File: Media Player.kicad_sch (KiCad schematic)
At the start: 74 parts, among them J1 PH2.0, J2 MEM2075-00-140-01-A, J3 USB_C_Receptacle_USB2.0_16P, J4 UART, Q2 DMP3068L-7, Q3 DMP3068L-7, SW1 BOOT, SW2 RESET, SW3 SW_Push, SW4 SW_Push, SW5 SW_Push, SW6 SW_Push, SW7 SW_SPST, U1 ESP32-S3-WROOM-1

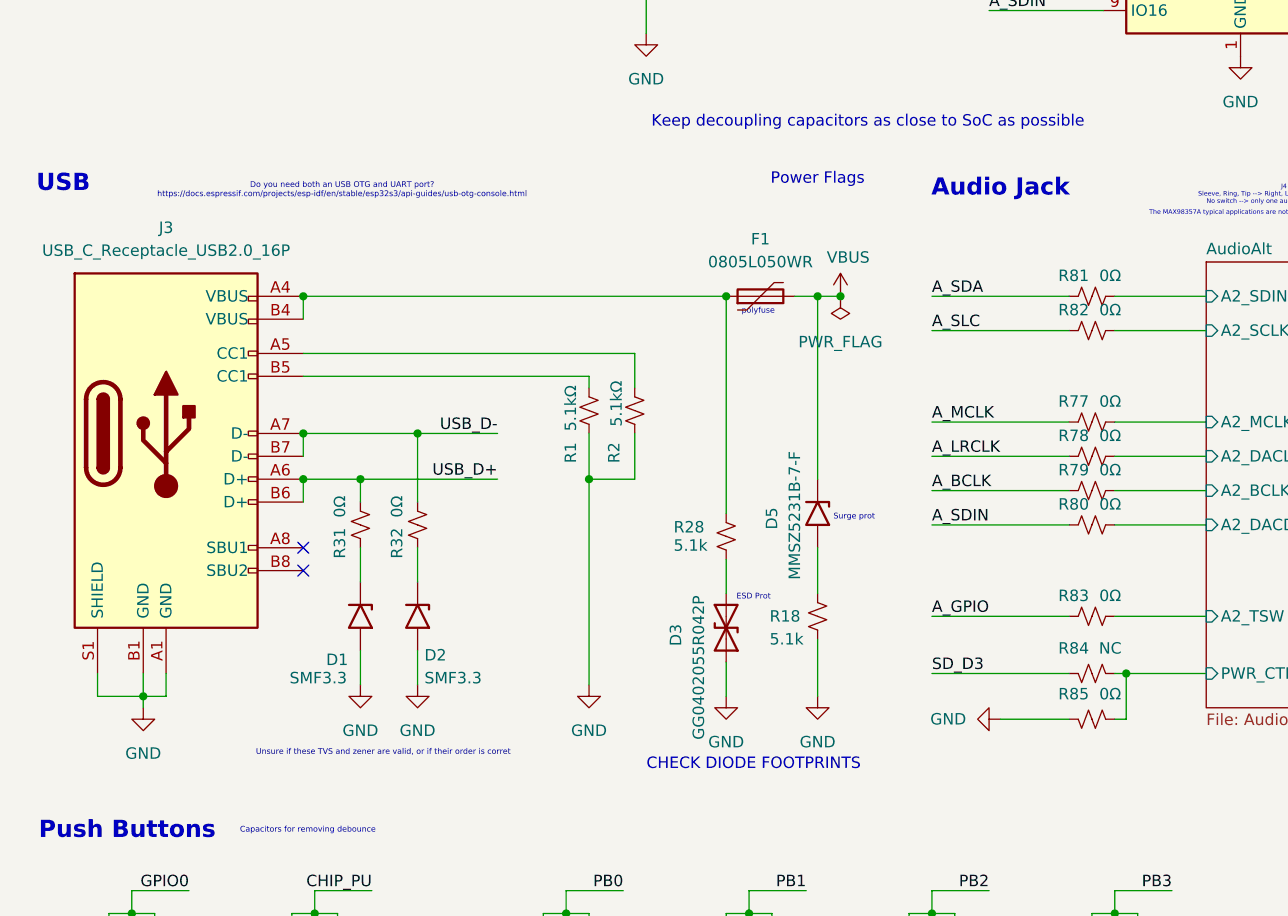
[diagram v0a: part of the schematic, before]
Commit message: Small Change to USB routing
Removed 0 resistors and change components to match reference schematic
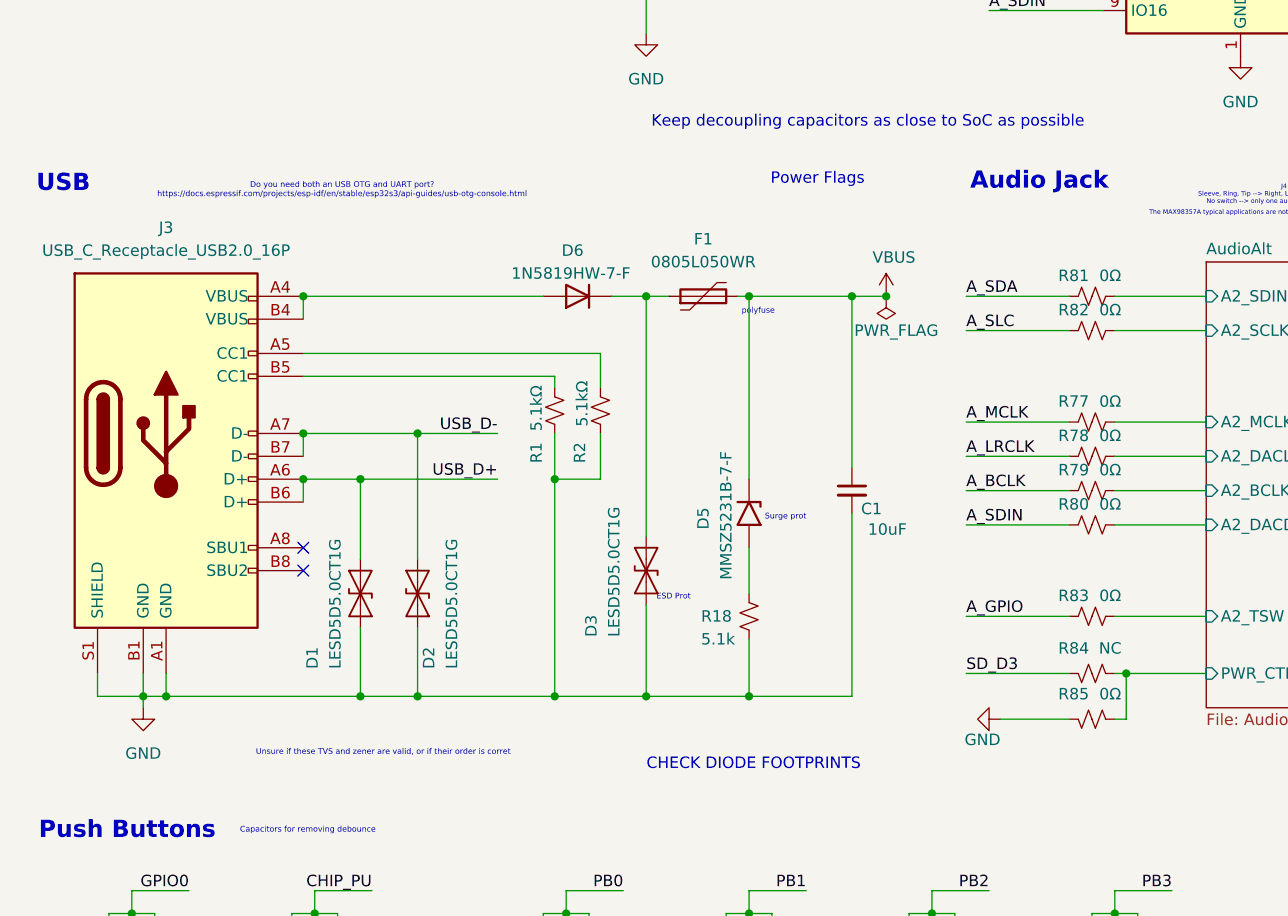
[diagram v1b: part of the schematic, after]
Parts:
- removed D1: SMF3.3, Diode_SMD:D_SOD-123F, symbol Diode:SMF33A
- removed D3: GG0402055R042P, Diode_SMD:D_0805_2012Metric_Pad1.15x1.40mm_HandSolder, symbol Diode:1.5KExxCA
- removed R28: 5.1k, Resistor_SMD:R_0805_2012Metric, symbol Device:R_Small_US
- removed R31, R32: 0Ω, Resistor_SMD:R_0805_2012Metric, symbol Device:R_Small_US
- added C1: 10uF, Capacitor_SMD:C_0805_2012Metric_Pad1.18x1.45mm_HandSolder, symbol Device:C_Small
- added D1, D3: LESD5D5.0CT1G, Diode_SMD:D_SMA, symbol Diode:SMAJ400CA
- added D6: 1N5819HW-7-F, Diode_SMD:D_SOD-123, symbol Device:D
- D2: value SMF3.3 -> LESD5D5.0CT1G; footprint Diode_SMD:D_SOD-123F -> Diode_SMD:D_SMA; symbol Diode:SMF33A -> Diode:SMAJ400CA
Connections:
- net GND: now also C1.2, D1.2 (A2), D3.2 (A2)
- net USB_D+: now also D1.1 (A1)
- net USB_D-: now also D2.1 (A1)
- net VBUS: now also C1.1
- net at J3.A4 (VBUS), J3.A9 (VBUS), J3.B4 (VBUS)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: now also D6.2 (A); no longer F1.1
- new net: D3.1 (A1), D6.1 (K), F1.1
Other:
- moved on the sheet: D5, F1, R1, R18, R2

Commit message: Compacting part 1
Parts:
- renumbered C1 to C0, dC13 to C1, dC10 to C10, dC1 to C2, C19 to C3, C12 to C30, C14 to C31, C15 to C32, C16 to C33, C17 to C34, C18 to C35, C33 to C36, dC11 to C40, D6 to D0, D5 to D4, F1 to F0, J3 to J1, J2 to J10, J1 to J40, J4 to J41, Q2 to Q10, Q3 to Q40, R18 to R0, R5 to R11, R6 to R12, R7 to R13, R8 to R14, R9 to R15, R24 to R16, R25 to R17, R26 to R18, R27 to R19, R56 to R20, R57 to R21, R53 to R22, R58 to R23, R4 to R3, R59 to R47, R54 to R48, R81 to R86, R82 to R87, R77 to R88, R78 to R89, R79 to R90, R80 to R91, R83 to R92, R84 to R93, R85 to R94, SW1 to SW30, SW2 to SW31, SW3 to SW32, SW4 to SW33, SW5 to SW34, SW6 to SW35, SW7 to SW36
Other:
- note added: "0-9"
- note added: "10-29"
- note added: "30-39"
- note added: "40-49"
- note added: "50-69"
- note removed: "Add mosfets on power rails to allow for controlling peripheral shutdown power saving"
- note removed: "Find Diode Footprints, + Fuse Confirm all IC footprints validity Do Decaps need smaller footprints?"
- note removed: "Is PSRAM in the WROOM S3? What do they need? Bring out the strapping pins and unused pins using test pad Bring the pull up on SD lines into the SD rules area Add zero resistors to the audio page + LCD + Power pages or connections coming out, additionally to all pins you are unsure of The PWR_ON_n signal is sus! When you turn of the device, is VSRC grounded? Wouldn't that make it always on? Read t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"
- moved on the sheet: D0

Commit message: JLC Design restraints
Updated design rules with JLC PCB. Combined numbers from Phils Lab and GPT for beginner friendly values (first board)
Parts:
- J1: value USB_C_Receptacle_USB2.0_16P -> 12402012E212A
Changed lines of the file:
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@@
 			)
 		)
-		(property "Value" "USB_C_Receptacle_USB2.0_16P"
+		(property "Value" "12402012E212A"
 			(at 31.75 104.14 0)
 			(effects

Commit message: Layout Draft 2, or almost
Charger layout based off of reference. Used more copper regions rather than traces. Other traces like buttons and test pads routed. Tried my best to make it all look good and parallel.

Added more silkscreen and logo.

STILL NEED TO DO POWER PLANE.
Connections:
- net USB_PWR: now reaches D0.2 (A), J1.A4 (VBUS), J1.A9 (VBUS), J1.B4 (VBUS), J1.B9 (VBUS)
- net USB_PWR2: now reaches D0.1 (K), D3.1 (A1), F0.1
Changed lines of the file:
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@@
+		)
+	)
+	(label "USB_PWR2"
+		(at 69.85 109.22 0)
+		(effects
+			(font
+				(size 1.27 1.27)
+			)
+			(justify left bottom)
 		)
 	)
@@
 		(effects
 			(font
+				(size 1.27 1.27)
+			)
+			(justify left bottom)
+		)
+	)
+	(label "USB_PWR"
+		(at 48.26 109.22 0)
+		(effects
+			(font
